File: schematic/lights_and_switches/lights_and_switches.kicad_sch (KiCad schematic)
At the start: 1 part

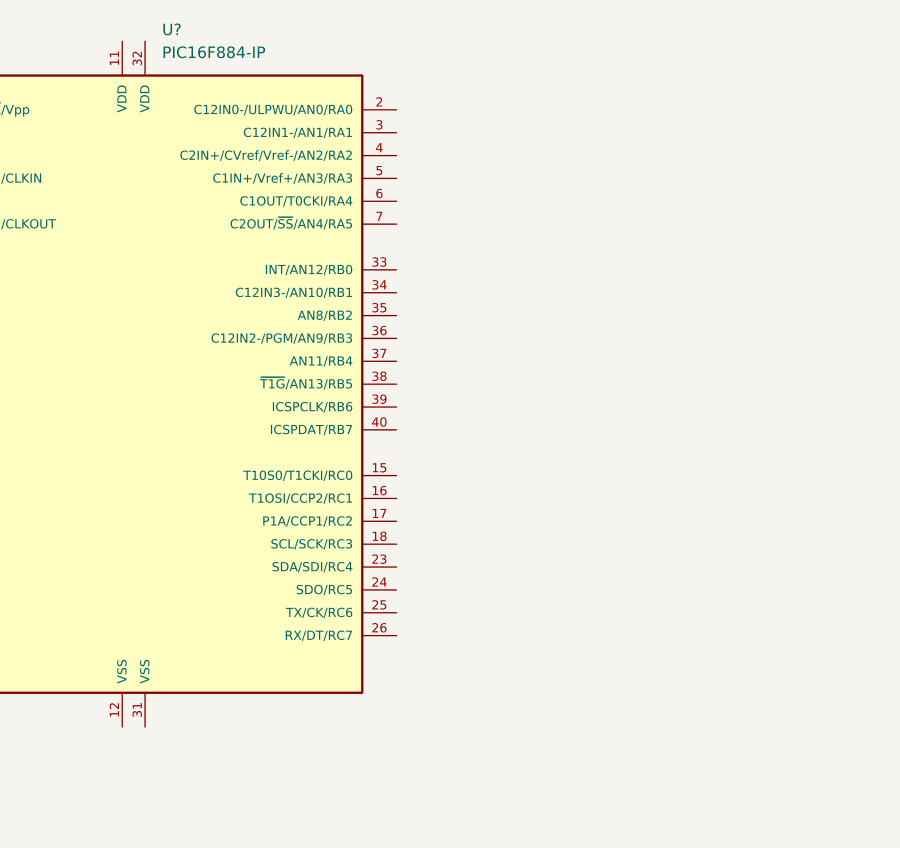
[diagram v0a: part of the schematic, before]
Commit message: Programmed device using PICkit3
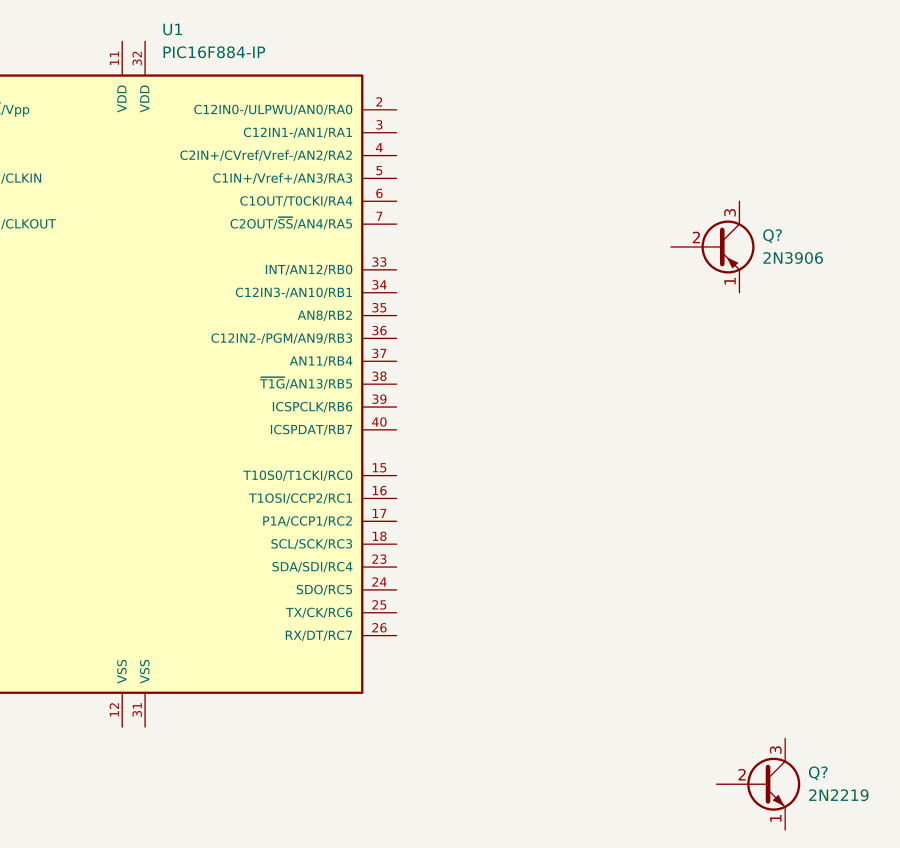
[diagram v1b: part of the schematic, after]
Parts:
- added Q?: 2N2219, Package_TO_SOT_THT:TO-39-3, symbol Transistor_BJT:2N2219
- added Q?: 2N3906, Package_TO_SOT_THT:TO-92_Inline, symbol Transistor_BJT:2N3906
- gave numbers to parts that had none: 1
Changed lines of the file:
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@@
   (symbol (lib_id "MCU_Microchip_PIC16:PIC16F884-IP") (at 128.27 82.55 0) (unit 1)
     (in_bom yes) (on_board yes) (fields_autoplaced)
-    (property "Reference" "U?" (id 0) (at 130.1497 43.18 0)
+    (property "Reference" "U1" (id 0) (at 130.1497 43.18 0)
       (effects (font (size 1.27 1.27)) (justify left))
     )
@@
     (pin "9")
   )
+  (symbol (lib_id "Transistor_BJT:2N2219") (at 196.85 127 0) (unit 1)
+    (in_bom yes) (on_board yes) (fields_autoplaced)
+    (property "Reference" "Q?" (id 0) (at 201.93 125.7299 0)
+      (effects (font (size 1.27 1.27)) (justify left))
+    )
+    (property "Value" "2N2219" (id 1) (at 201.93 128.2699 0)
+      (effects (font (size 1.27 1.27)) (justify left))
+    )
+    (property "Footprint" "Package_TO_SOT_THT:TO-39-3" (id 2) (at 201.93 128.905 0)
+      (effects (font (size 1.27 1.27) italic) (justify left) hide)
+    )
+    (property "Datasheet" "http://www.onsemi.com/pub_link/Collateral/2N2219-D.PDF" (id 3) (at 196.85 127 0)
+      (effects (font (size 1.27 1.27)) (justify left) hide)
+    )
+    (pin "1")
+    (pin "2")
+    (pin "3")
+  )
+  (symbol (lib_id "Transistor_BJT:2N3906") (at 191.77 67.31 0) (unit 1)
+    (in_bom yes) (on_board yes) (fields_autoplaced)
+    (property "Reference" "Q?" (id 0) (at 196.85 66.0399 0)
+      (effects (font (size 1.27 1.27)) (justify left))
+    )
+    (property "Value" "2N3906" (id 1) (at 196.85 68.5799 0)
+      (effects (font (size 1.27 1.27)) (justify left))
+    )
+    (property "Footprint" "Package_TO_SOT_THT:TO-92_Inline" (id 2) (at 196.85 69.215 0)
+      (effects (font (size 1.27 1.27) italic) (justify left) hide)
+    )
+    (property "Datasheet" "https://www.onsemi.com/pub/Collateral/2N3906-D.PDF" (id 3) (at 191.77 67.31 0)
+      (effects (font (size 1.27 1.27)) (justify left) hide)
+    )
+    (pin "1")
+    (pin "2")
+    (pin "3")
+  )
   (sheet_instances
     (path "/" (page "1"))
   )
   (symbol_instances
+    (path "/8153434b-5ee3-45ac-b0e2-dd937fdd246f"
+      (reference "Q?") (unit 1) (value "2N2219") (footprint "Package_TO_SOT_THT:TO-39-3")
+    )
+    (path "/9f9b037b-a248-426c-ae3e-f105bd37f00a"
+      (reference "Q?") (unit 1) (value "2N3906") (footprint "Package_TO_SOT_THT:TO-92_Inline")
+    )
     (path "/5338134d-a05d-4ad9-9bd6-6a3cccd5d5a9"
-      (reference "U?") (unit 1) (value "PIC16F884-IP") (footprint "")
+      (reference "U1") (unit 1) (value "PIC16F884-IP") (footprint "")
     )
   )

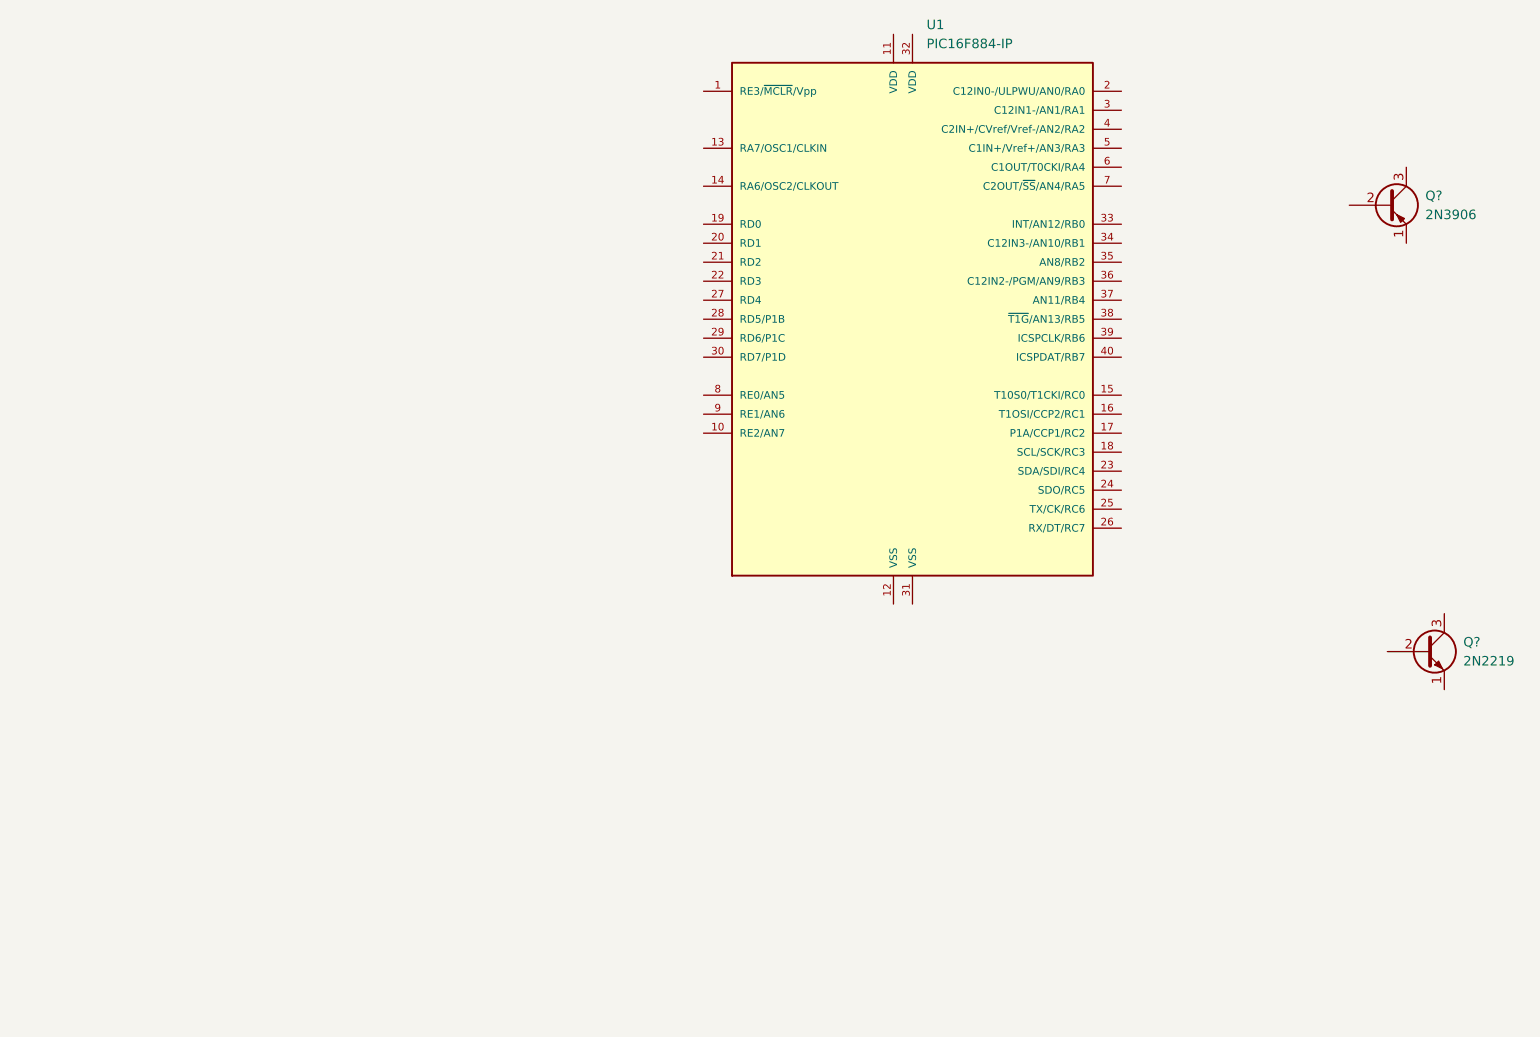
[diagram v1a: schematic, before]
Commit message: Updating to newer MPLABX IDE and adding details to schematic
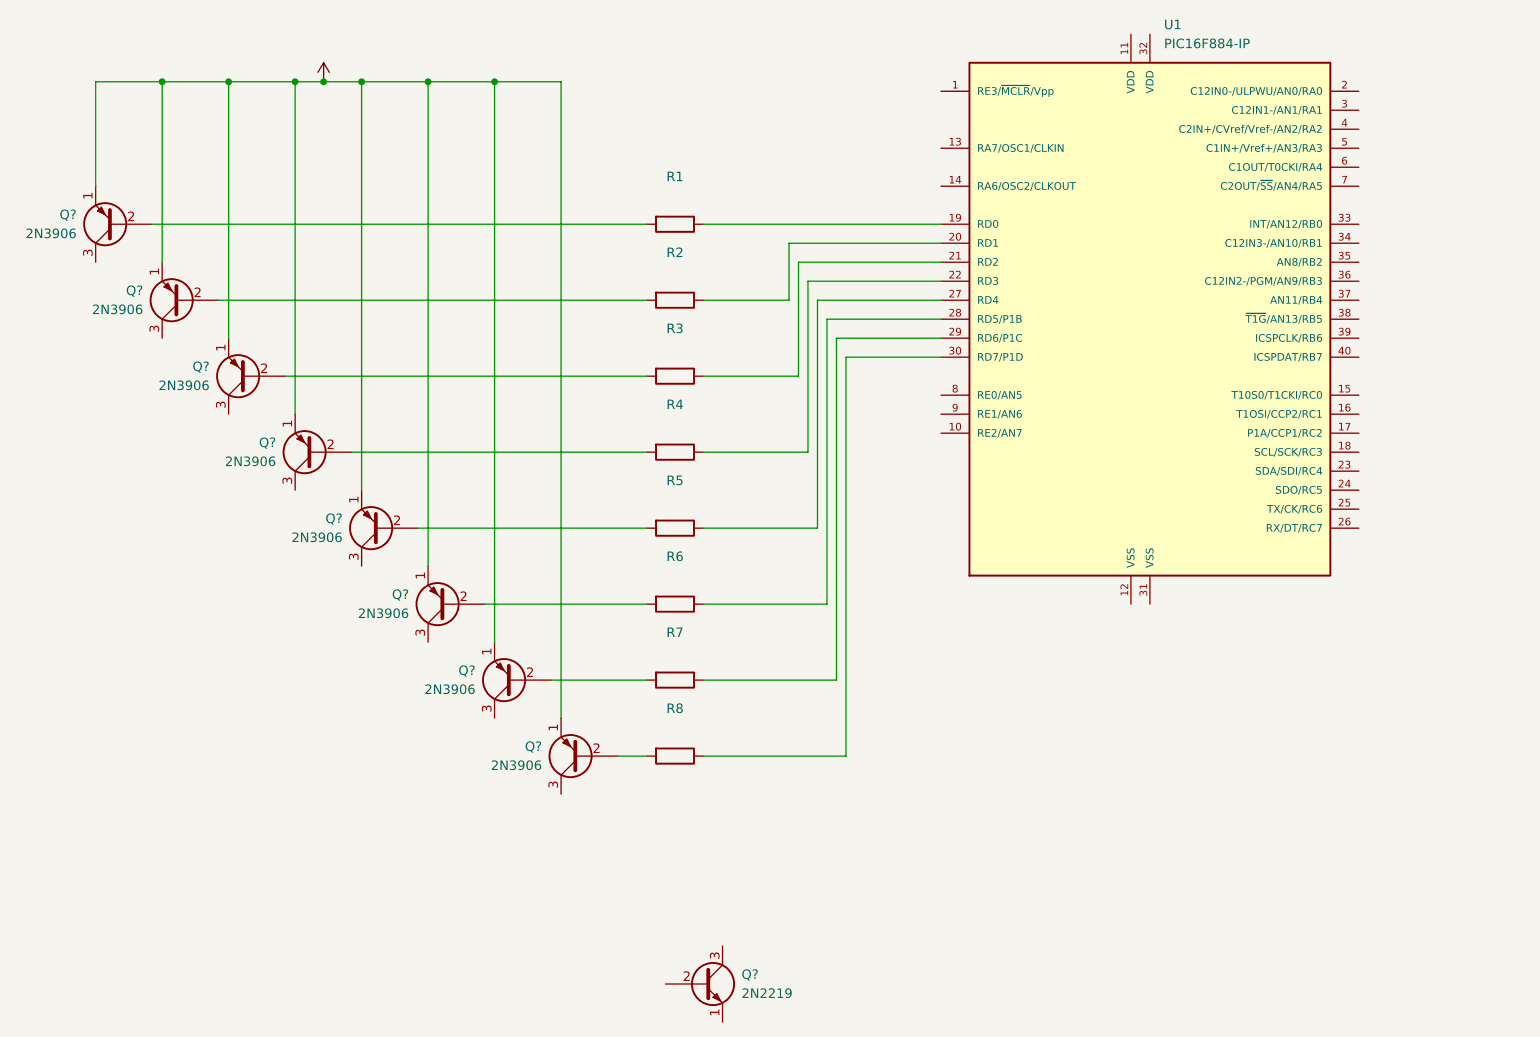
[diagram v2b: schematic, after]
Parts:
- added Q? (x7): 2N3906, Package_TO_SOT_THT:TO-92_Inline, symbol Transistor_BJT:2N3906
- added R1, R2, R3, R4, R5, R6, R7, R8: (no value), symbol Device:R
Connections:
- net at U1.19 (RD0): now also R1.1
- net at U1.20 (RD1): now also R2.1
- net at U1.21 (RD2): now also R3.1
- net at U1.22 (RD3): now also R4.1
- net at U1.27 (RD4): now also R5.1
- net at U1.28 (RD5/P1B): now also R6.1
- net at U1.29 (RD6/P1C): now also R7.1
- net at U1.30 (RD7/P1D): now also R8.1
- net +5V: now reaches Q?.1 (E)
- net +5V: now also Q?.1 (E), Q?.1 (E), Q?.1 (E), Q?.1 (E), Q?.1 (E), Q?.1 (E), Q?.1 (E)
- net at Q?.2 (B): now also R1.2
- new net: Q?.2 (B), R7.2
- new net: Q?.2 (B), R2.2
- new net: Q?.2 (B), R5.2
- new net: Q?.2 (B), R3.2
- new net: Q?.2 (B), R8.2
- new net: Q?.2 (B), R6.2
- new net: Q?.2 (B), R4.2
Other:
- moved on the sheet: Q?, U1

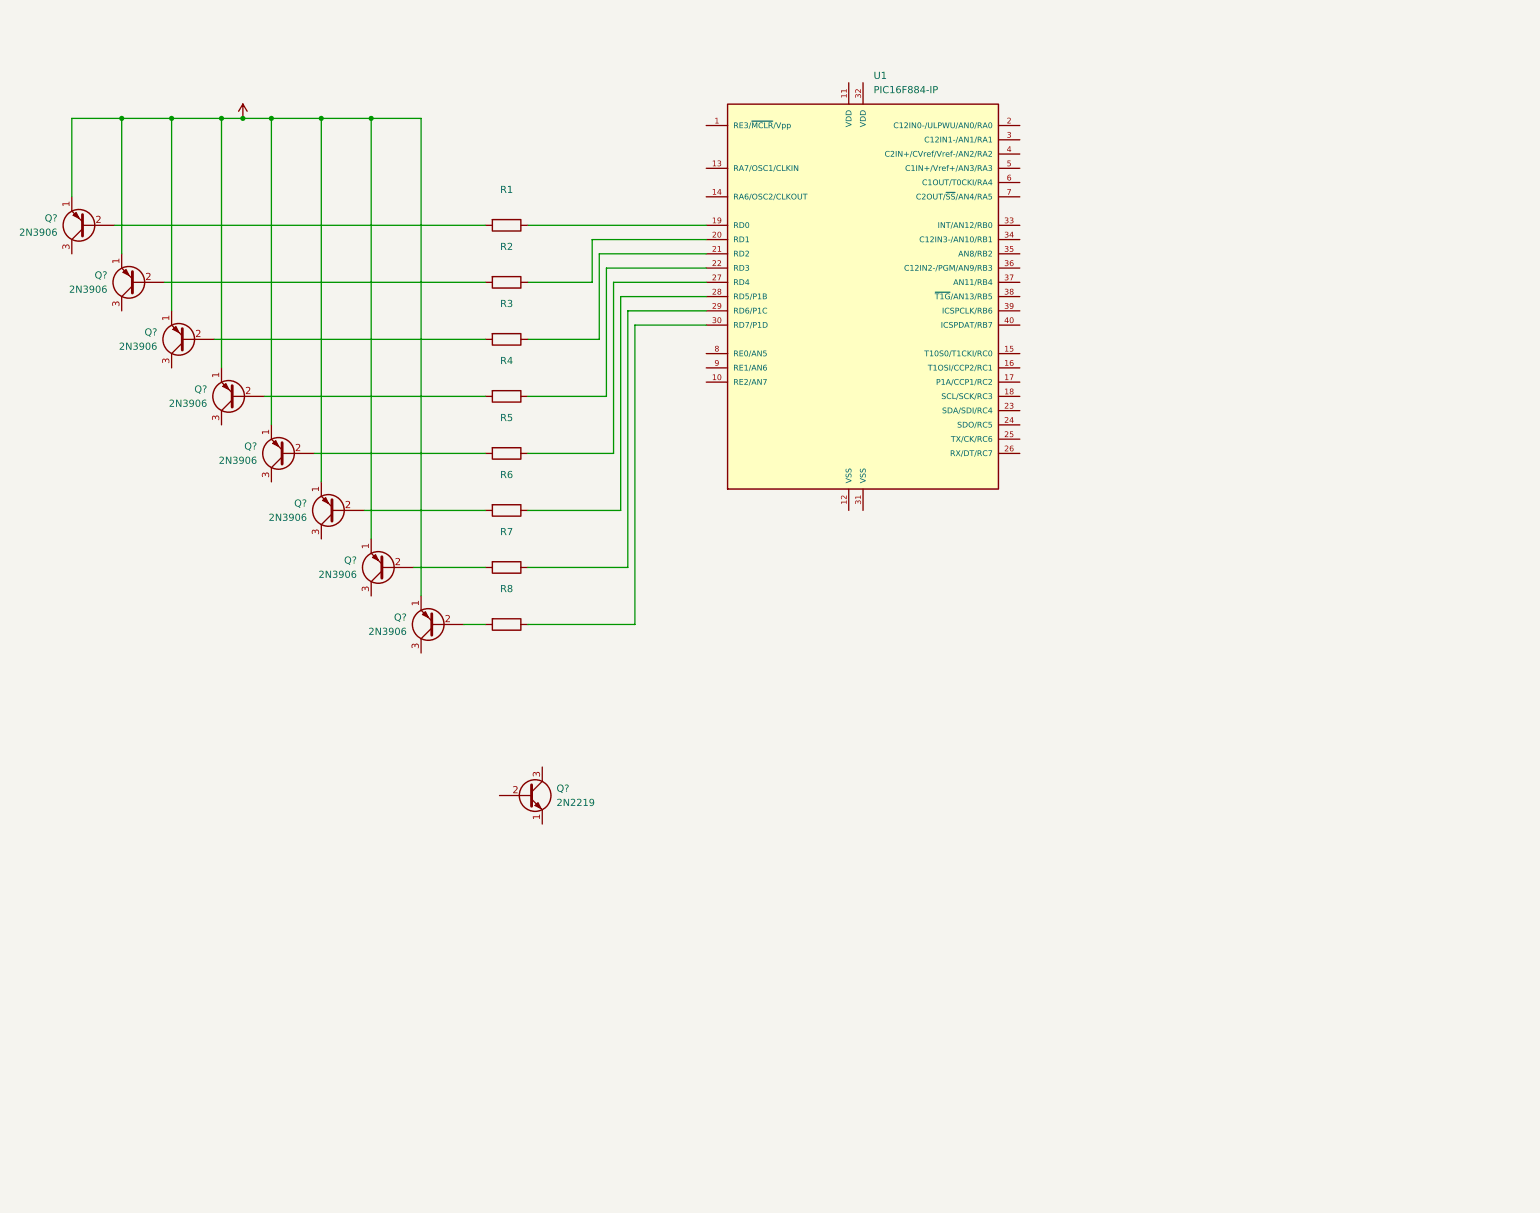
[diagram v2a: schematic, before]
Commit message: Updating diagram
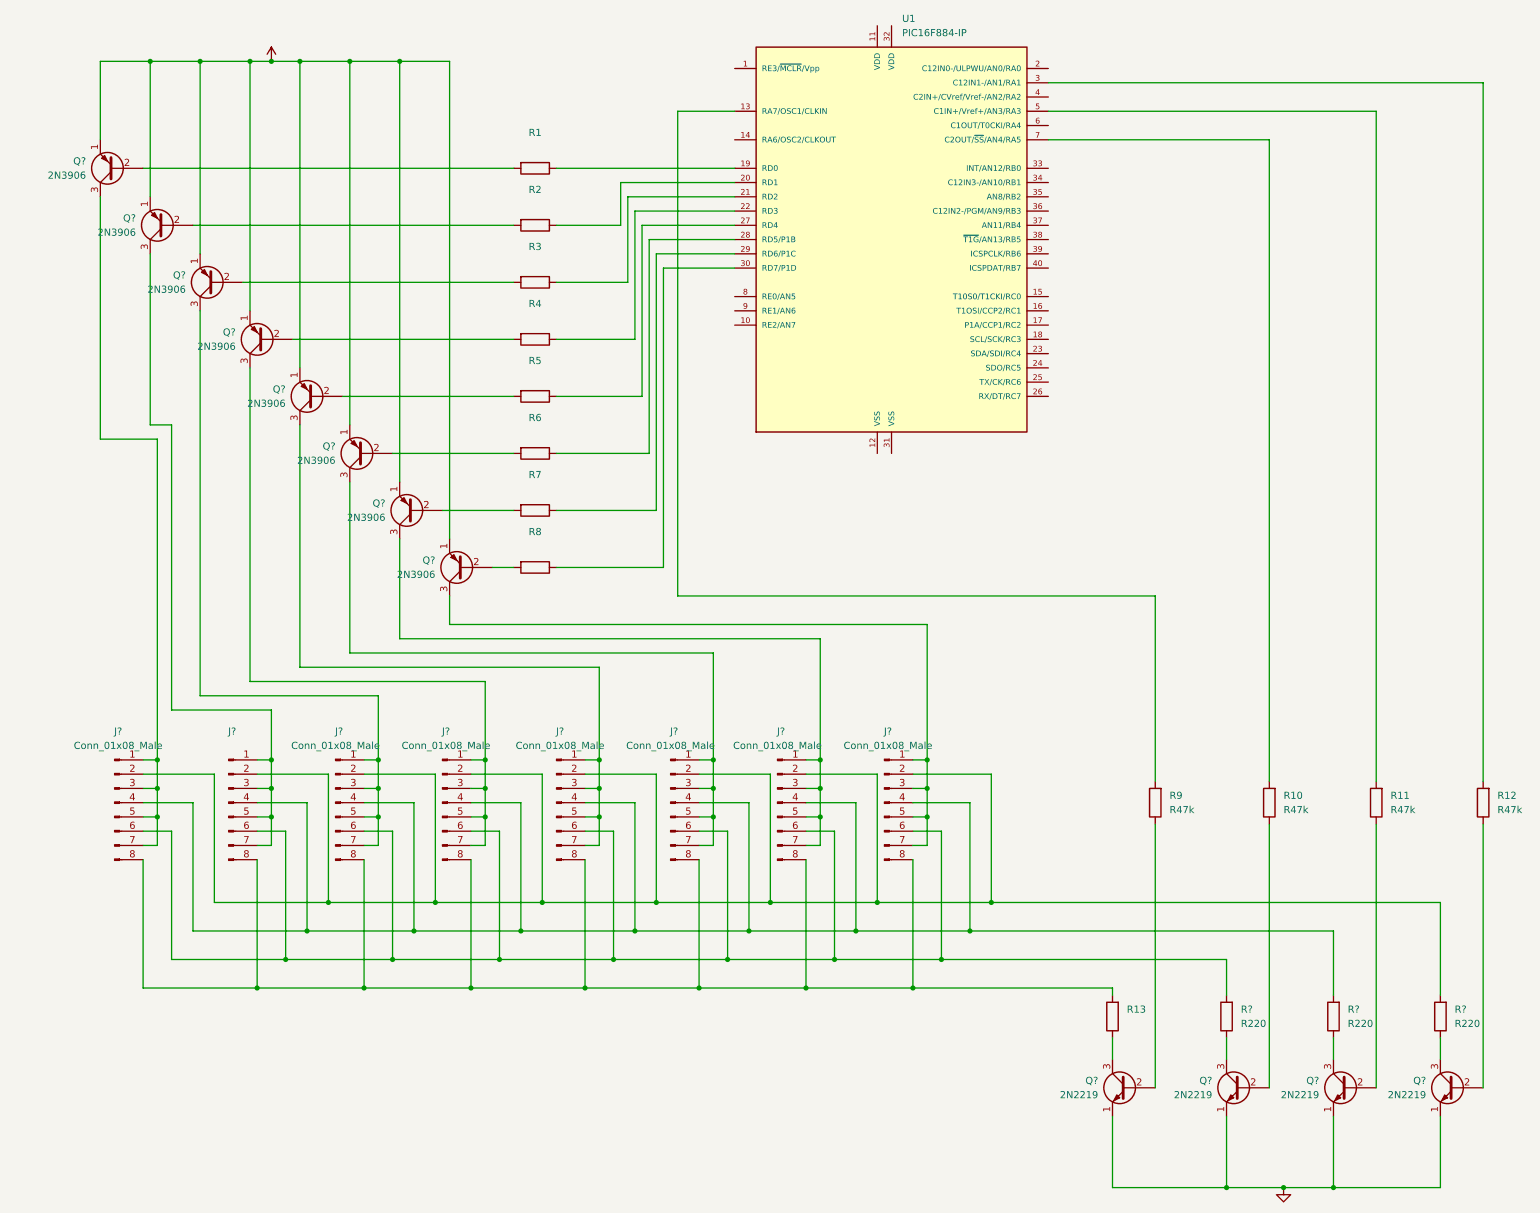
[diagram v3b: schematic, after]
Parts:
- added J? (x7): Conn_01x08_Male, Connector_PinHeader_2.54mm:PinHeader_1x08_P2.54mm_Vertical, symbol Connector:Conn_01x08_Male
- added J?: (no value), symbol Connector:Conn_01x08_Male
- added Q? (x3): 2N2219, Package_TO_SOT_THT:TO-39-3, symbol Transistor_BJT:2N2219
- added R10, R11, R12, R9: R47k, symbol Device:R
- added R13: (no value), symbol Device:R
- added R? (x3): R220, symbol Device:R
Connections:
- net at U1.13 (RA7/OSC1/CLKIN): now also R9.2
- net at U1.3 (C12IN1-/AN1/RA1): now also R12.2
- net at U1.5 (C1IN+/Vref+/AN3/RA3): now also R11.2
- net at U1.7 (C2OUT/~{SS}/AN4/RA5): now also R10.2
- net at Q?.3 (C): now also J?.1 (Pin_1), J?.3 (Pin_3), J?.5 (Pin_5), J?.7 (Pin_7) (x8)
- net GND: now reaches Q?.1 (E)
- net GND: now also Q?.1 (E), Q?.1 (E), Q?.1 (E)
- net at Q?.2 (B): now also R9.1
- net at Q?.3 (C): now also R13.1
- new net: J?.2 (Pin_2), J?.2 (Pin_2), J?.2 (Pin_2), J?.2 (Pin_2), J?.2 (Pin_2), J?.2 (Pin_2), J?.2 (Pin_2), J?.2 (Pin_2), R?.2
- new net: J?.4 (Pin_4), J?.4 (Pin_4), J?.4 (Pin_4), J?.4 (Pin_4), J?.4 (Pin_4), J?.4 (Pin_4), J?.4 (Pin_4), J?.4 (Pin_4), R?.2
- new net: J?.6 (Pin_6), J?.6 (Pin_6), J?.6 (Pin_6), J?.6 (Pin_6), J?.6 (Pin_6), J?.6 (Pin_6), J?.6 (Pin_6), J?.6 (Pin_6), R?.2
- new net: J?.8 (Pin_8), J?.8 (Pin_8), J?.8 (Pin_8), J?.8 (Pin_8), J?.8 (Pin_8), J?.8 (Pin_8), J?.8 (Pin_8), J?.8 (Pin_8), R13.2
- new net: Q?.2 (B), R11.1
- new net: Q?.3 (C), R?.1 (x3)
- new net: Q?.2 (B), R10.1
- new net: Q?.2 (B), R12.1
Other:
- moved on the sheet: Q?, R1, R2, R3, R4, R5, R6, R7, R8, U1
